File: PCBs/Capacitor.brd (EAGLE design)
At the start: 15 x 42 mm, 3 parts

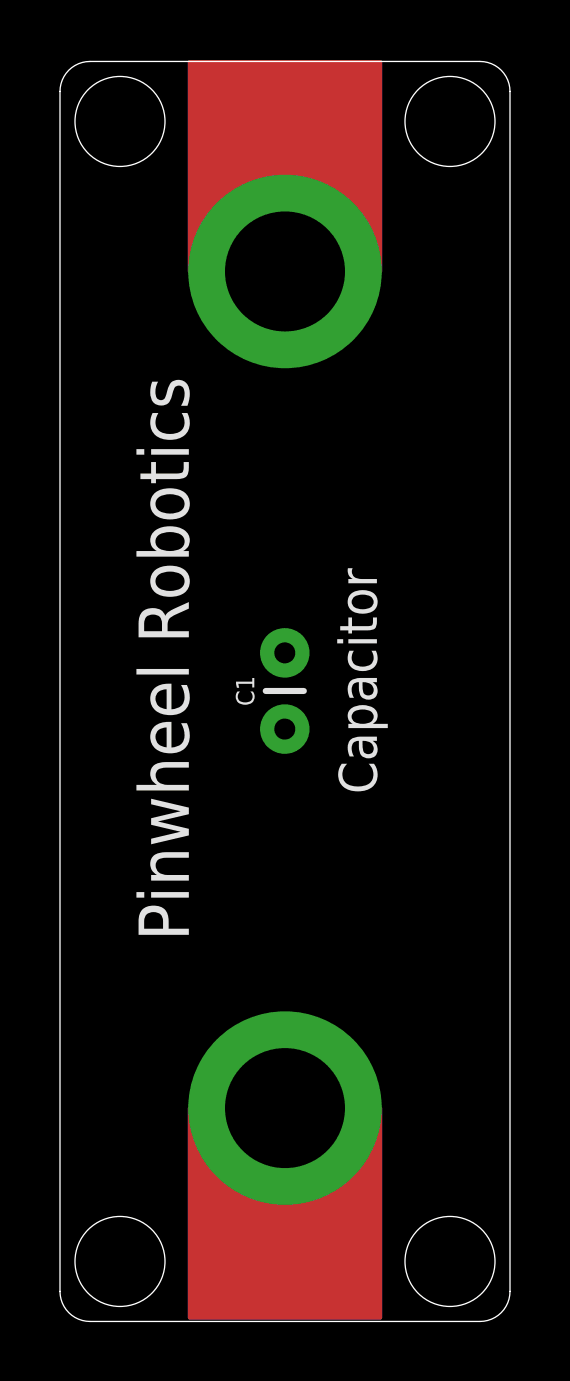
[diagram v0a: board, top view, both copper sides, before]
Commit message: Update for Dim width is 42 length is 28 for type 2 pcb
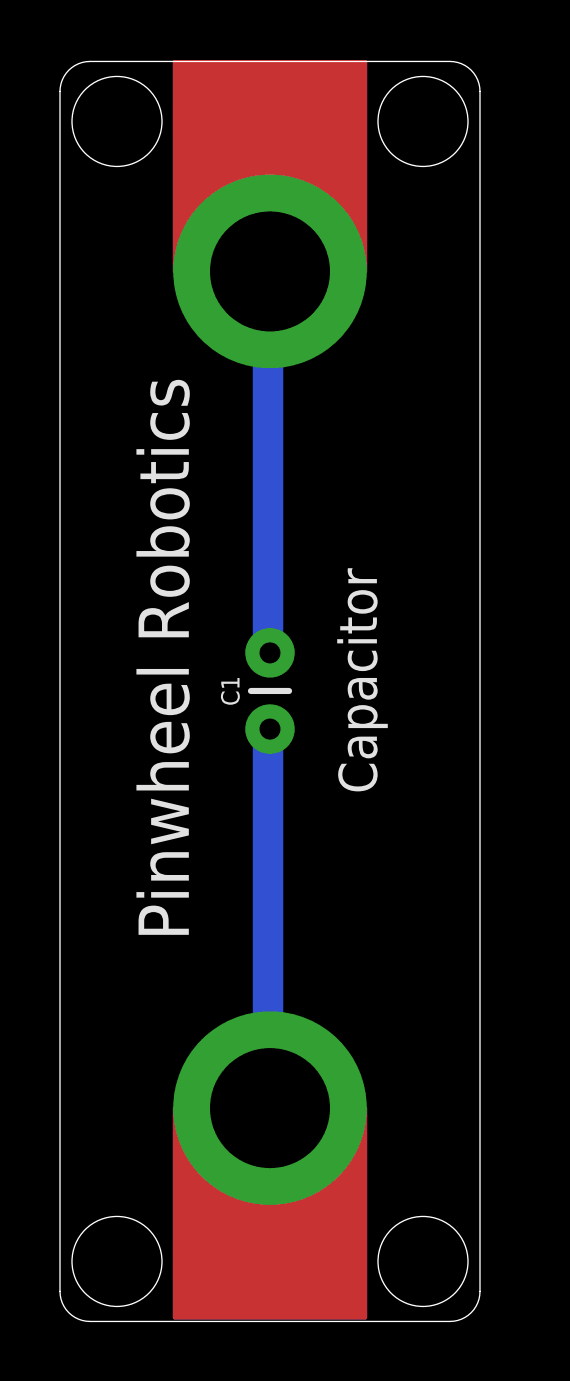
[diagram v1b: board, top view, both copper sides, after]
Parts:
- moved U$1 0.50 mm to (7.00, 35.0)
- moved U$2 0.50 mm to (7.00, 7.11)
- moved C1 0.49 mm to (7.00, 21.0)
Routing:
- net N$2: track 0.00 -> 12.7 mm
- net N$1: track 0.00 -> 12.7 mm
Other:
- board size 15 x 42 mm -> 14 x 42 mm
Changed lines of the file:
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@@
 <drawing>
 <settings>
-<setting alwaysvectorfont="yes"/>
+<setting alwaysvectorfont="no"/>
 <setting verticaltext="up"/>
 </settings>
@@
 <wire x1="0" y1="41" x2="0" y2="1" width="0" layer="20"/>
 <wire x1="0" y1="1" x2="1" y2="0" width="0" layer="20" curve="90"/>
-<wire x1="1" y1="0" x2="14" y2="0" width="0" layer="20"/>
-<wire x1="14" y1="0" x2="15" y2="1" width="0" layer="20" curve="90"/>
-<wire x1="15" y1="1" x2="15" y2="41" width="0" layer="20"/>
-<wire x1="15" y1="41" x2="14" y2="42" width="0" layer="20" curve="90"/>
-<wire x1="14" y1="42" x2="1" y2="42" width="0" layer="20"/>
+<wire x1="1" y1="0" x2="13" y2="0" width="0" layer="20"/>
+<wire x1="13" y1="0" x2="14" y2="1" width="0" layer="20" curve="90"/>
+<wire x1="14" y1="1" x2="14" y2="41" width="0" layer="20"/>
+<wire x1="14" y1="41" x2="13" y2="42" width="0" layer="20" curve="90"/>
+<wire x1="13" y1="42" x2="1" y2="42" width="0" layer="20"/>
 <wire x1="1" y1="42" x2="0" y2="41" width="0" layer="20" curve="90"/>
 <text x="4.295" y="12.684" size="1.6764" layer="21" rot="R90">Pinwheel Robotics </text>
 <text x="10.564" y="17.581" size="1.27" layer="21" rot="R90">Capacitor</text>
-<hole x="2" y="40" drill="3"/>
-<hole x="13" y="40" drill="3"/>
-<hole x="2" y="2" drill="3"/>
-<hole x="13" y="2" drill="3"/>
+<hole x="1.9" y="40" drill="3"/>
+<hole x="12.1" y="40" drill="3"/>
+<hole x="1.9" y="2" drill="3"/>
+<hole x="12.1" y="2" drill="3"/>
 <text x="13.103" y="31.54" size="1.778" layer="22" rot="MR270">care@pinwheel.in</text>
 <dimension x1="-3" y1="42" x2="-3" y2="0" x3="-13.5" y3="21" textsize="1.778" layer="1"/>
 <dimension x1="0" y1="42.5" x2="15" y2="42.5" x3="7.5" y3="48" textsize="1.778" layer="1"/>
+<dimension x1="0" y1="44" x2="14" y2="44" x3="7" y3="43.5" textsize="1.778" layer="1"/>
+<dimension x1="15.5" y1="2" x2="15.5" y2="40" x3="14" y3="21" textsize="1.778" layer="1"/>
 </plain>
 <attributes>
@@
 </autorouter>
 <elements>
-<element name="C1" library="SparkFun-Capacitors" library_urn="urn:adsk.eagle:library:510" package="CAP-PTH-2.54" package3d_urn="urn:adsk.eagle:package:37435/1" value="22pF" x="7.493" y="21.016" smashed="yes" rot="R90">
-<attribute name="NAME" x="6.477" y="21.016" size="0.6096" layer="25" font="vector" ratio="20" rot="R90" align="bottom-center"/>
-<attribute name="PROD_ID" value="CAP-09128" x="25.273" y="36.256" size="1.778" layer="27" rot="R90" display="off"/>
-<attribute name="VALUE" x="8.509" y="21.016" size="0.6096" layer="27" font="vector" ratio="20" rot="R90" align="top-center"/>
+<element name="C1" library="SparkFun-Capacitors" library_urn="urn:adsk.eagle:library:510" package="CAP-PTH-2.54" package3d_urn="urn:adsk.eagle:package:37435/1" value="22pF" x="7" y="21.016" smashed="yes" rot="R90">
+<attribute name="NAME" x="5.984" y="21.016" size="0.6096" layer="25" font="vector" ratio="20" rot="R90" align="bottom-center"/>
+<attribute name="PROD_ID" value="CAP-09128" x="24.78" y="36.256" size="1.778" layer="27" rot="R90" display="off"/>
+<attribute name="VALUE" x="8.016" y="21.016" size="0.6096" layer="27" font="vector" ratio="20" rot="R90" align="top-center"/>
 </element>
-<element name="U$1" library="microbit" package="MICROBIT_PAD" value="MICROBIT_PAD" x="7.5" y="35" smashed="yes" rot="R180"/>
-<element name="U$2" library="microbit" package="MICROBIT_PAD" value="MICROBIT_PAD" x="7.5" y="7.112" smashed="yes"/>
+<element name="U$1" library="microbit" package="MICROBIT_PAD" value="MICROBIT_PAD" x="7" y="35" smashed="yes" rot="R180"/>
+<element name="U$2" library="microbit" package="MICROBIT_PAD" value="MICROBIT_PAD" x="7" y="7.112" smashed="yes"/>
 </elements>
 <signals>
@@
 <contactref element="C1" pad="1"/>
 <contactref element="U$2" pad="PAD"/>
-<wire x1="7.5" y1="7.112" x2="7.493" y2="19.746" width="0" layer="19" extent="1-1"/>
+<wire x1="6.9342" y1="7.2644" x2="6.9342" y2="19.4818" width="1.016" layer="16"/>
+<wire x1="6.9342" y1="19.4818" x2="7" y2="19.746" width="0.508" layer="16"/>
+<wire x1="6.9342" y1="7.2644" x2="7" y2="7.112" width="0.508" layer="16"/>
 </signal>
 <signal name="N$2">
 <contactref element="U$1" pad="PAD"/>
 <contactref element="C1" pad="2"/>
-<wire x1="7.493" y1="22.286" x2="7.5" y2="35" width="0" layer="19" extent="1-1"/>
+<wire x1="6.9342" y1="34.671" x2="6.9342" y2="22.4536" width="1.016" layer="16"/>
+<wire x1="6.9342" y1="22.4536" x2="7" y2="22.286" width="0.508" layer="16"/>
+<wire x1="6.9342" y1="34.671" x2="7" y2="35" width="0.508" layer="16"/>
 </signal>
 </signals>

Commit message: Corrected hole position for some design , made transistor as switch as category 1
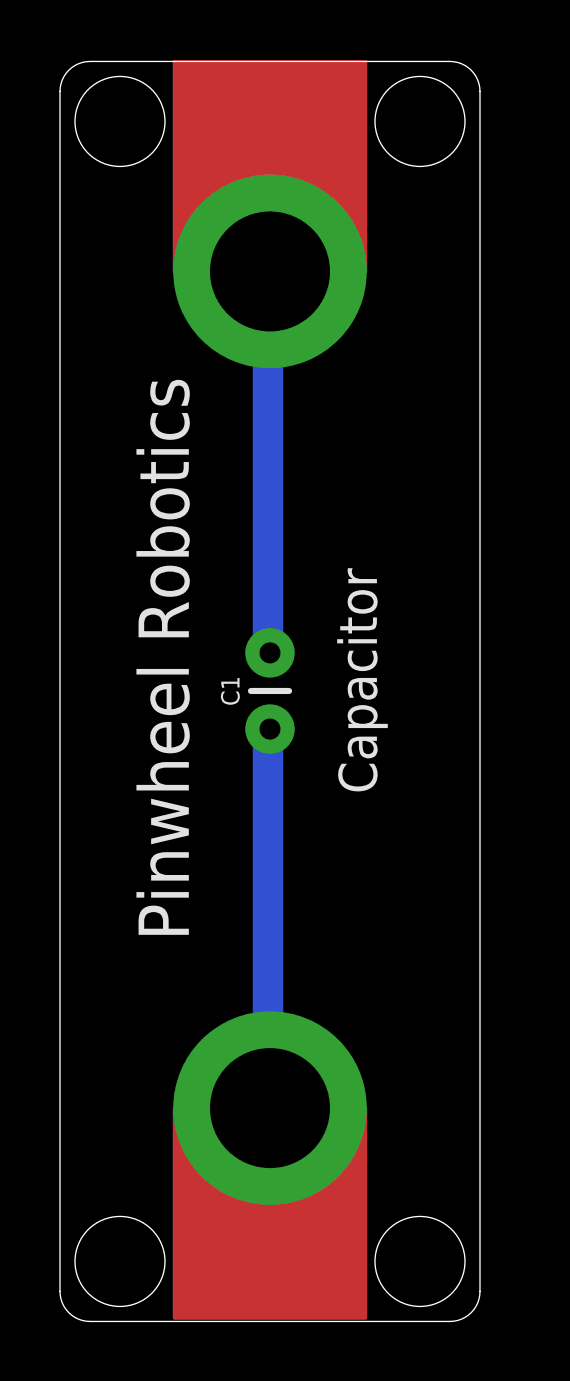
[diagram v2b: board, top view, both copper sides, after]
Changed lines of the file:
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@@
 <text x="4.295" y="12.684" size="1.6764" layer="21" rot="R90">Pinwheel Robotics </text>
 <text x="10.564" y="17.581" size="1.27" layer="21" rot="R90">Capacitor</text>
-<hole x="1.9" y="40" drill="3"/>
-<hole x="12.1" y="40" drill="3"/>
-<hole x="1.9" y="2" drill="3"/>
-<hole x="12.1" y="2" drill="3"/>
+<hole x="2" y="40" drill="3"/>
+<hole x="12" y="40" drill="3"/>
+<hole x="2" y="2" drill="3"/>
+<hole x="12" y="2" drill="3"/>
 <text x="13.103" y="31.54" size="1.778" layer="22" rot="MR270">care@pinwheel.in</text>
 <dimension x1="-3" y1="42" x2="-3" y2="0" x3="-13.5" y3="21" textsize="1.778" layer="1"/>
